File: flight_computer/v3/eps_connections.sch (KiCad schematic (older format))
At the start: 27 parts, among them J15 Power, J16 Power, J18 Power, J19 Power, J20 BUSS+, J21 EPS Serial, J22 Power, Q1 BSS138, Q2 BSS138, Q3 BSS138

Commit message: Updating based on harnesses
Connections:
- net +3V3: now also J19.2 (Pin_2); no longer J19.1 (Pin_1)
- net +5V: now also J21.6 (Pin_6), J22.2 (Pin_2); no longer J21.1 (Pin_1), J22.1 (Pin_1)
- net GND: now also J15.1 (Pin_1), J16.1 (Pin_1), J18.1 (Pin_1), J19.1 (Pin_1), J21.2 (Pin_2), J22.1 (Pin_1); no longer J15.2 (Pin_2), J16.2 (Pin_2), J18.2 (Pin_2), J19.2 (Pin_2), J21.5 (Pin_5), J22.2 (Pin_2)
- net VBUS: now also J18.2 (Pin_2); no longer J18.1 (Pin_1)
- net VDDF: now also J16.2 (Pin_2); no longer J16.1 (Pin_1)
- net VPP: now also J15.2 (Pin_2); no longer J15.1 (Pin_1)
- net at Q3.3 (D), R80.1: now also J21.5 (Pin_5); no longer J21.2 (Pin_2)
- net at Q2.3 (D), R77.1: now also J21.4 (Pin_4); no longer J21.3 (Pin_3)
- net at Q1.3 (D), R75.1: now also J21.3 (Pin_3); no longer J21.4 (Pin_4)
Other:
- moved on the sheet: C100, C101, C104
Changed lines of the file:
@@
 L Connector:Conn_01x06_Male J?
 U 1 1 64D96689
-P 7500 3450
+P 7500 3550
 AR Path="/64D823E8/64D96689" Ref="J?"  Part="1"
 AR Path="/64D821F3/64D96689" Ref="J21"  Part="1"
-F 0 "J21" H 7400 3550 50  0000 C CNN
-F 1 "EPS Serial" H 7250 3450 50  0000 C CNN
-F 2 "Connector_Hirose:Hirose_DF13C_CL535-0406-3-51_1x06-1MP_P1.25mm_Vertical" H 7500 3450 50  0001 C CNN
-F 3 "~" H 7500 3450 50  0001 C CNN
-	1    7500 3450
-	-1   0    0    -1
+F 0 "J21" H 7400 3650 50  0000 C CNN
+F 1 "EPS Serial" H 7250 3550 50  0000 C CNN
+F 2 "Connector_Hirose:Hirose_DF13C_CL535-0406-3-51_1x06-1MP_P1.25mm_Vertical" H 7500 3550 50  0001 C CNN
+F 3 "~" H 7500 3550 50  0001 C CNN
+	1    7500 3550
+	-1   0    0    1
 $EndComp
 $Comp
 L Connector:Conn_01x02_Male J?
 U 1 1 64D9668F
-P 7500 4550
+P 7500 4650
 AR Path="/64D823E8/64D9668F" Ref="J?"  Part="1"
 AR Path="/64D821F3/64D9668F" Ref="J22"  Part="1"
-F 0 "J22" H 7472 4524 50  0000 R CNN
-F 1 "Power" H 7472 4433 50  0000 R CNN
-F 2 "Connector_Hirose:Hirose_DF13C_CL535-0402-2-51_1x02-1MP_P1.25mm_Vertical" H 7500 4550 50  0001 C CNN
-F 3 "~" H 7500 4550 50  0001 C CNN
-	1    7500 4550
-	-1   0    0    -1
+F 0 "J22" H 7472 4624 50  0000 R CNN
+F 1 "Power" H 7472 4533 50  0000 R CNN
+F 2 "Connector_Hirose:Hirose_DF13C_CL535-0402-2-51_1x02-1MP_P1.25mm_Vertical" H 7500 4650 50  0001 C CNN
+F 3 "~" H 7500 4650 50  0001 C CNN
+	1    7500 4650
+	-1   0    0    1
 $EndComp
 $Comp
@@
 L Connector:Conn_01x02_Male J?
 U 1 1 64D97269
-P 6900 4550
+P 6900 4650
 AR Path="/64D823E8/64D97269" Ref="J?"  Part="1"
 AR Path="/64D821F3/64D97269" Ref="J19"  Part="1"
-F 0 "J19" H 6872 4524 50  0000 R CNN
-F 1 "Power" H 6872 4433 50  0000 R CNN
-F 2 "Connector_Hirose:Hirose_DF13C_CL535-0402-2-51_1x02-1MP_P1.25mm_Vertical" H 6900 4550 50  0001 C CNN
-F 3 "~" H 6900 4550 50  0001 C CNN
-	1    6900 4550
-	-1   0    0    -1
+F 0 "J19" H 6872 4624 50  0000 R CNN
+F 1 "Power" H 6872 4533 50  0000 R CNN
+F 2 "Connector_Hirose:Hirose_DF13C_CL535-0402-2-51_1x02-1MP_P1.25mm_Vertical" H 6900 4650 50  0001 C CNN
+F 3 "~" H 6900 4650 50  0001 C CNN
+	1    6900 4650
+	-1   0    0    1
 $EndComp
 $Comp
@@
 L Connector:Conn_01x02_Male J?
 U 1 1 64D986CF
-P 6300 4550
+P 6300 4650
 AR Path="/64D823E8/64D986CF" Ref="J?"  Part="1"
 AR Path="/64D821F3/64D986CF" Ref="J18"  Part="1"
-F 0 "J18" H 6272 4524 50  0000 R CNN
-F 1 "Power" H 6272 4433 50  0000 R CNN
-F 2 "Connector_Hirose:Hirose_DF13C_CL535-0402-2-51_1x02-1MP_P1.25mm_Vertical" H 6300 4550 50  0001 C CNN
-F 3 "~" H 6300 4550 50  0001 C CNN
-	1    6300 4550
-	-1   0    0    -1
+F 0 "J18" H 6272 4624 50  0000 R CNN
+F 1 "Power" H 6272 4533 50  0000 R CNN
+F 2 "Connector_Hirose:Hirose_DF13C_CL535-0402-2-51_1x02-1MP_P1.25mm_Vertical" H 6300 4650 50  0001 C CNN
+F 3 "~" H 6300 4650 50  0001 C CNN
+	1    6300 4650
+	-1   0    0    1
 $EndComp
 $Comp
@@
 L Device:C C104
 U 1 1 64DFB3B8
-P 5450 5500
-F 0 "C104" H 5565 5546 50  0000 L CNN
-F 1 "0.1u" H 5565 5455 50  0000 L CNN
-F 2 "Capacitor_SMD:C_0603_1608Metric" H 5488 5350 50  0001 C CNN
-F 3 "~" H 5450 5500 50  0001 C CNN
-	1    5450 5500
+P 5400 5500
+F 0 "C104" H 5515 5546 50  0000 L CNN
+F 1 "0.1u" H 5515 5455 50  0000 L CNN
+F 2 "Capacitor_SMD:C_0603_1608Metric" H 5438 5350 50  0001 C CNN
+F 3 "~" H 5400 5500 50  0001 C CNN
+	1    5400 5500
 	1    0    0    -1
 $EndComp
@@
 L power:GND #PWR?
 U 1 1 64DFB3BE
-P 5450 5650
+P 5400 5650
 AR Path="/6313FC31/64DFB3BE" Ref="#PWR?"  Part="1"
 AR Path="/64DFB3BE" Ref="#PWR?"  Part="1"
@@
 AR Path="/64D823E8/64DFB3BE" Ref="#PWR?"  Part="1"
 AR Path="/64D821F3/64DFB3BE" Ref="#PWR0332"  Part="1"
-F 0 "#PWR0332" H 5450 5400 50  0001 C CNN
-F 1 "GND" H 5455 5477 50  0000 C CNN
-F 2 "" H 5450 5650 50  0001 C CNN
-F 3 "" H 5450 5650 50  0001 C CNN
-	1    5450 5650
+F 0 "#PWR0332" H 5400 5400 50  0001 C CNN
+F 1 "GND" H 5405 5477 50  0000 C CNN
+F 2 "" H 5400 5650 50  0001 C CNN
+F 3 "" H 5400 5650 50  0001 C CNN
+	1    5400 5650
 	1    0    0    -1
 $EndComp
@@
 L power:+5V #PWR?
 U 1 1 64DFC12D
-P 5450 5350
+P 5400 5350
 AR Path="/64D823E8/64DFC12D" Ref="#PWR?"  Part="1"
 AR Path="/64D821F3/64DFC12D" Ref="#PWR0331"  Part="1"
-F 0 "#PWR0331" H 5450 5200 50  0001 C CNN
-F 1 "+5V" H 5465 5523 50  0000 C CNN
-F 2 "" H 5450 5350 50  0001 C CNN
-F 3 "" H 5450 5350 50  0001 C CNN
-	1    5450 5350
+F 0 "#PWR0331" H 5400 5200 50  0001 C CNN
+F 1 "+5V" H 5415 5523 50  0000 C CNN
+F 2 "" H 5400 5350 50  0001 C CNN
+F 3 "" H 5400 5350 50  0001 C CNN
+	1    5400 5350
 	1    0    0    -1
 $EndComp
@@
 L Connector:Conn_01x02_Male J?
 U 1 1 66862097
-P 5050 4550
+P 5050 4650
 AR Path="/64D823E8/66862097" Ref="J?"  Part="1"
 AR Path="/64D821F3/66862097" Ref="J16"  Part="1"
-F 0 "J16" H 5022 4524 50  0000 R CNN
-F 1 "Power" H 5022 4433 50  0000 R CNN
-F 2 "Connector_Hirose:Hirose_DF13C_CL535-0402-2-51_1x02-1MP_P1.25mm_Vertical" H 5050 4550 50  0001 C CNN
-F 3 "~" H 5050 4550 50  0001 C CNN
-	1    5050 4550
-	-1   0    0    -1
+F 0 "J16" H 5022 4624 50  0000 R CNN
+F 1 "Power" H 5022 4533 50  0000 R CNN
+F 2 "Connector_Hirose:Hirose_DF13C_CL535-0402-2-51_1x02-1MP_P1.25mm_Vertical" H 5050 4650 50  0001 C CNN
+F 3 "~" H 5050 4650 50  0001 C CNN
+	1    5050 4650
+	-1   0    0    1
 $EndComp
 $Comp
@@
 L Device:C C101
 U 1 1 668B2DCA
-P 4250 5500
-F 0 "C101" H 4365 5546 50  0000 L CNN
-F 1 "0.1u" H 4365 5455 50  0000 L CNN
-F 2 "Capacitor_SMD:C_0603_1608Metric" H 4288 5350 50  0001 C CNN
-F 3 "~" H 4250 5500 50  0001 C CNN
-	1    4250 5500
+P 5000 5500
+F 0 "C101" H 5115 5546 50  0000 L CNN
+F 1 "0.1u" H 5115 5455 50  0000 L CNN
+F 2 "Capacitor_SMD:C_0603_1608Metric" H 5038 5350 50  0001 C CNN
+F 3 "~" H 5000 5500 50  0001 C CNN
+	1    5000 5500
 	1    0    0    -1
 $EndComp
@@
 L power:GND #PWR?
 U 1 1 668B2DD0
-P 4250 5650
+P 5000 5650
 AR Path="/6313FC31/668B2DD0" Ref="#PWR?"  Part="1"
 AR Path="/668B2DD0" Ref="#PWR?"  Part="1"
@@
 AR Path="/64D823E8/668B2DD0" Ref="#PWR?"  Part="1"
 AR Path="/64D821F3/668B2DD0" Ref="#PWR0322"  Part="1"
-F 0 "#PWR0322" H 4250 5400 50  0001 C CNN
-F 1 "GND" H 4255 5477 50  0000 C CNN
-F 2 "" H 4250 5650 50  0001 C CNN
-F 3 "" H 4250 5650 50  0001 C CNN
-	1    4250 5650
+F 0 "#PWR0322" H 5000 5400 50  0001 C CNN
+F 1 "GND" H 5005 5477 50  0000 C CNN
+F 2 "" H 5000 5650 50  0001 C CNN
+F 3 "" H 5000 5650 50  0001 C CNN
+	1    5000 5650
 	1    0    0    -1
 $EndComp
@@
 L Device:C C100
 U 1 1 668B2DDC
-P 3850 5500
-F 0 "C100" H 3965 5546 50  0000 L CNN
-F 1 "10u" H 3965 5455 50  0000 L CNN
-F 2 "Capacitor_SMD:C_0603_1608Metric" H 3888 5350 50  0001 C CNN
-F 3 "~" H 3850 5500 50  0001 C CNN
-	1    3850 5500
+P 4600 5500
+F 0 "C100" H 4715 5546 50  0000 L CNN
+F 1 "10u" H 4715 5455 50  0000 L CNN
+F 2 "Capacitor_SMD:C_0603_1608Metric" H 4638 5350 50  0001 C CNN
+F 3 "~" H 4600 5500 50  0001 C CNN
+	1    4600 5500
 	1    0    0    -1
 $EndComp
@@
 L power:GND #PWR?
 U 1 1 668B2DE2
-P 3850 5650
+P 4600 5650
 AR Path="/6313FC31/668B2DE2" Ref="#PWR?"  Part="1"
 AR Path="/668B2DE2" Ref="#PWR?"  Part="1"
@@
 AR Path="/64D823E8/668B2DE2" Ref="#PWR?"  Part="1"
 AR Path="/64D821F3/668B2DE2" Ref="#PWR0318"  Part="1"
-F 0 "#PWR0318" H 3850 5400 50  0001 C CNN
-F 1 "GND" H 3855 5477 50  0000 C CNN
-F 2 "" H 3850 5650 50  0001 C CNN
-F 3 "" H 3850 5650 50  0001 C CNN
-	1    3850 5650
+F 0 "#PWR0318" H 4600 5400 50  0001 C CNN
+F 1 "GND" H 4605 5477 50  0000 C CNN
+F 2 "" H 4600 5650 50  0001 C CNN
+F 3 "" H 4600 5650 50  0001 C CNN
+	1    4600 5650
 	1    0    0    -1
 $EndComp
@@
 L power:VDDF #PWR0317
 U 1 1 668B3D40
-P 3850 5350
-F 0 "#PWR0317" H 3850 5200 50  0001 C CNN
-F 1 "VDDF" H 3865 5523 50  0000 C CNN
-F 2 "" H 3850 5350 50  0001 C CNN
-F 3 "" H 3850 5350 50  0001 C CNN
-	1    3850 5350
+P 4600 5350
+F 0 "#PWR0317" H 4600 5200 50  0001 C CNN
+F 1 "VDDF" H 4615 5523 50  0000 C CNN
+F 2 "" H 4600 5350 50  0001 C CNN
+F 3 "" H 4600 5350 50  0001 C CNN
+	1    4600 5350
 	1    0    0    -1
 $EndComp
@@
 L Connector:Conn_01x02_Male J?
 U 1 1 668D93A8
-P 4400 4550
+P 4400 4650
 AR Path="/64D823E8/668D93A8" Ref="J?"  Part="1"
 AR Path="/64D821F3/668D93A8" Ref="J15"  Part="1"
-F 0 "J15" H 4372 4524 50  0000 R CNN
-F 1 "Power" H 4372 4433 50  0000 R CNN
-F 2 "Connector_Hirose:Hirose_DF13C_CL535-0402-2-51_1x02-1MP_P1.25mm_Vertical" H 4400 4550 50  0001 C CNN
-F 3 "~" H 4400 4550 50  0001 C CNN
-	1    4400 4550
-	-1   0    0    -1
+F 0 "J15" H 4372 4624 50  0000 R CNN
+F 1 "Power" H 4372 4533 50  0000 R CNN
+F 2 "Connector_Hirose:Hirose_DF13C_CL535-0402-2-51_1x02-1MP_P1.25mm_Vertical" H 4400 4650 50  0001 C CNN
+F 3 "~" H 4400 4650 50  0001 C CNN
+	1    4400 4650
+	-1   0    0    1
 $EndComp
 $Comp
@@
 L power:VPP #PWR0113
 U 1 1 64E8D40A
-P 4250 5350
-F 0 "#PWR0113" H 4250 5200 50  0001 C CNN
-F 1 "VPP" H 4265 5523 50  0000 C CNN
-F 2 "" H 4250 5350 50  0001 C CNN
-F 3 "" H 4250 5350 50  0001 C CNN
-	1    4250 5350
-	1    0    0    -1
-$EndComp
+P 5000 5350
+F 0 "#PWR0113" H 5000 5200 50  0001 C CNN
+F 1 "VPP" H 5015 5523 50  0000 C CNN
+F 2 "" H 5000 5350 50  0001 C CNN
+F 3 "" H 5000 5350 50  0001 C CNN
+	1    5000 5350
+	1    0    0    -1
+$EndComp

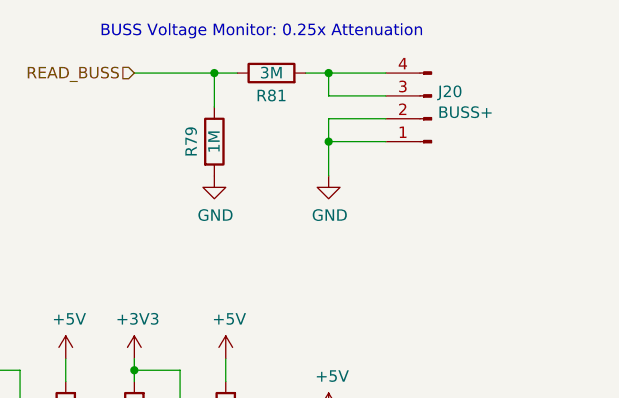
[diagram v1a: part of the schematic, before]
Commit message: Add silkscreen text
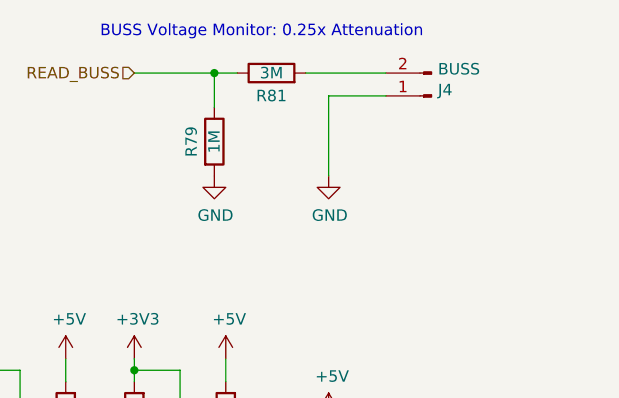
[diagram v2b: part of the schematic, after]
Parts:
- removed J20: BUSS+, Connector_Hirose:Hirose_DF13C_CL535-0404-8-51_1x04-1MP_P1.25mm_Vertical, symbol Connector:Conn_01x04_Male
- added J4: BUSS, Connector_Hirose:Hirose_DF13C_CL535-0402-2-51_1x02-1MP_P1.25mm_Vertical, symbol Connector:Conn_01x02_Male
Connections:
- net GND: now also J4.1 (Pin_1)
- net at R81.2: now also J4.2 (Pin_2)
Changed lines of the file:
@@
-$EndComp
-$Comp
-L Connector:Conn_01x04_Male J20
-U 1 1 66920F9B
-P 7500 1750
-F 0 "J20" H 7472 1632 50  0000 R CNN
-F 1 "BUSS+" H 7472 1723 50  0000 R CNN
-F 2 "Connector_Hirose:Hirose_DF13C_CL535-0404-8-51_1x04-1MP_P1.25mm_Vertical" H 7500 1750 50  0001 C CNN
-F 3 "~" H 7500 1750 50  0001 C CNN
-	1    7500 1750
-	-1   0    0    1
 $EndComp
 $Comp
@@
 $EndComp
 Wire Wire Line
-	7300 1750 7050 1750
-Wire Wire Line
-	7050 1750 7050 1850
-Wire Wire Line
-	7300 1850 7050 1850
-Connection ~ 7050 1850
-Wire Wire Line
-	7050 1850 7050 2000
+	7300 1650 7050 1650
 $Comp
 L Device:R R?
@@
 	6550 1550 6550 1700
 Wire Wire Line
-	6950 1550 7050 1550
-Wire Wire Line
-	7300 1650 7050 1650
-Wire Wire Line
-	7050 1650 7050 1550
-Connection ~ 7050 1550
-Wire Wire Line
-	7050 1550 7300 1550
-Wire Wire Line
 	6550 1550 6200 1550
 Connection ~ 6550 1550
@@
 	1    0    0    -1
 $EndComp
+Wire Wire Line
+	6950 1550 7300 1550
+$Comp
+L Connector:Conn_01x02_Male J?
+U 1 1 64F69F0E
+P 7500 1650
+AR Path="/64D823E8/64F69F0E" Ref="J?"  Part="1"
+AR Path="/64D821F3/64F69F0E" Ref="J4"  Part="1"
+F 0 "J4" H 7472 1624 50  0000 R CNN
+F 1 "BUSS" H 7472 1533 50  0000 R CNN
+F 2 "Connector_Hirose:Hirose_DF13C_CL535-0402-2-51_1x02-1MP_P1.25mm_Vertical" H 7500 1650 50  0001 C CNN
+F 3 "~" H 7500 1650 50  0001 C CNN
+	1    7500 1650
+	-1   0    0    1
+$EndComp
+Wire Wire Line
+	7050 1650 7050 2000
 $EndSCHEMATC
